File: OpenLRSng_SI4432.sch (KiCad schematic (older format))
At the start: 33 parts, among them IC1 ATMEGA328P-A, IC2 Si4432, P1 CONN_01X06, P2 CONN_02X06, P3 MML, U1 MIC5205 3,3V, Y1 RESONATEUR

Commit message: 100uF Cap von 1206 auf 1210 geändert
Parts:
- C12: footprint Capacitors_SMD:C_1206 -> Capacitors_SMD:C_1210
- C2: value 100µ -> 22u
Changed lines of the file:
@@
 LIBS:Resonator_3pins
 LIBS:OpenLRSng_SI4432-cache
-EELAYER 25 0
+EELAYER 24 0
 EELAYER END
 $Descr A4 11693 8268
@@
 P 1200 1550
 F 0 "C2" H 1200 1650 40  0000 L CNN
-F 1 "100µ" H 1206 1465 40  0000 L CNN
+F 1 "22u" H 1206 1465 40  0000 L CNN
 F 2 "Capacitors_SMD:C_1206" H 1238 1400 30  0000 C CNN
 F 3 "" H 1200 1550 60  0000 C CNN
@@
 F 0 "C12" H 6750 1200 40  0000 L CNN
 F 1 "100µ" H 6756 1015 40  0000 L CNN
-F 2 "Capacitors_SMD:C_1206" H 6788 950 30  0000 C CNN
+F 2 "Capacitors_SMD:C_1210" H 6788 950 30  0000 C CNN
 F 3 "" H 6750 1100 60  0000 C CNN
 	1    6750 1100

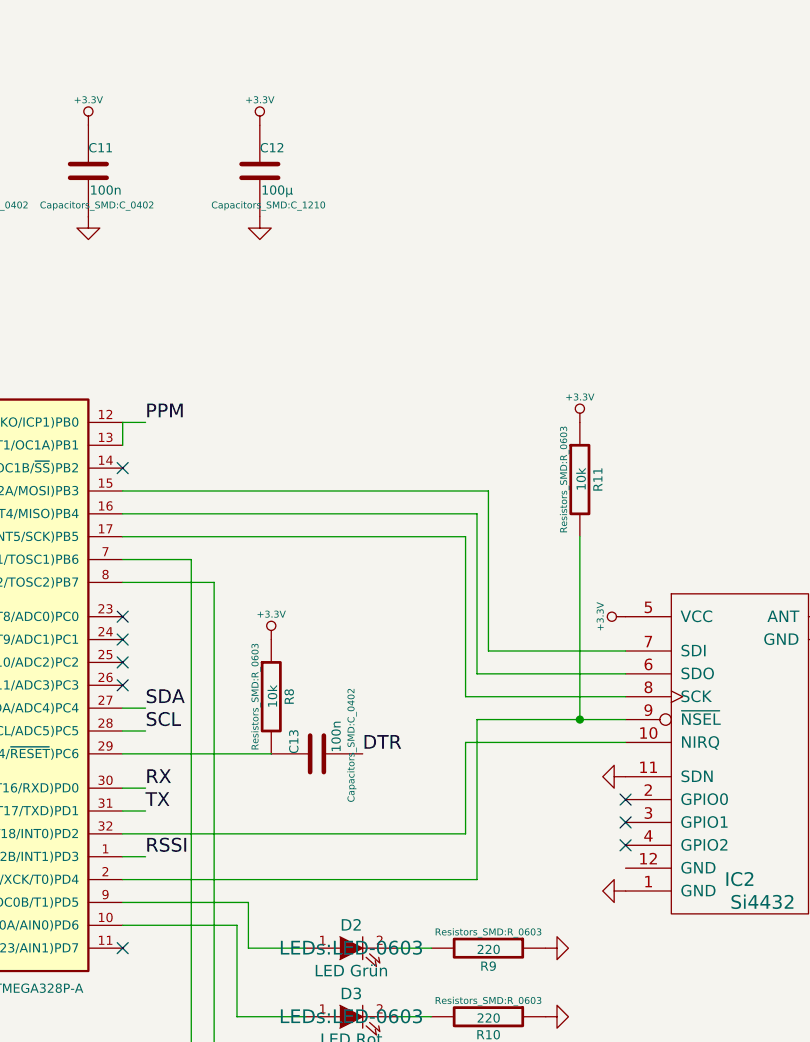
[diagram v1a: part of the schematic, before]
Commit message: -SI4432 Bibliothek gefixt (Pin14 GND vergessen im Schaltplan) -DuKo Kupferfläche vergrößert -zusätzlich noch einmal 100uF Kerko an die 3,3V Rail -Via Stichting an der Massefläche
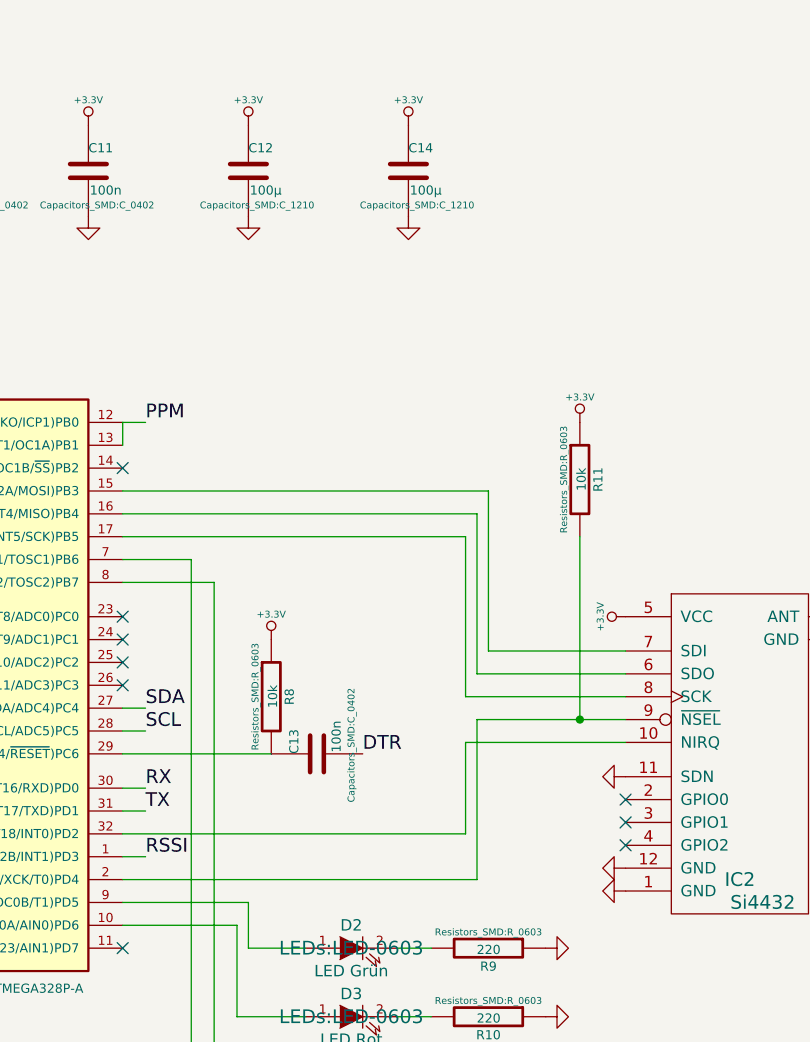
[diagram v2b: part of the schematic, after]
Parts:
- added C14: 100µ, Capacitors_SMD:C_1210, symbol C
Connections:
- net +3.3V: now also C14.1
- net GND: now also IC2.12 (GND), C14.2
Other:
- moved on the sheet: C12
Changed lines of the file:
@@
 LIBS:Resonator_3pins
 LIBS:OpenLRSng_SI4432-cache
-EELAYER 24 0
+EELAYER 25 0
 EELAYER END
 $Descr A4 11693 8268
@@
 L C C12
 U 1 1 54CDC71D
-P 6750 1100
-F 0 "C12" H 6750 1200 40  0000 L CNN
-F 1 "100µ" H 6756 1015 40  0000 L CNN
-F 2 "Capacitors_SMD:C_1210" H 6788 950 30  0000 C CNN
-F 3 "" H 6750 1100 60  0000 C CNN
-	1    6750 1100
+P 6700 1100
+F 0 "C12" H 6700 1200 40  0000 L CNN
+F 1 "100µ" H 6706 1015 40  0000 L CNN
+F 2 "Capacitors_SMD:C_1210" H 6738 950 30  0000 C CNN
+F 3 "" H 6700 1100 60  0000 C CNN
+	1    6700 1100
 	1    0    0    -1
 $EndComp
@@
 L GND #PWR045
 U 1 1 54CDCEDD
-P 6750 1300
-F 0 "#PWR045" H 6750 1300 30  0001 C CNN
-F 1 "GND" H 6750 1230 30  0001 C CNN
-F 2 "" H 6750 1300 60  0000 C CNN
-F 3 "" H 6750 1300 60  0000 C CNN
-	1    6750 1300
+P 6700 1300
+F 0 "#PWR045" H 6700 1300 30  0001 C CNN
+F 1 "GND" H 6700 1230 30  0001 C CNN
+F 2 "" H 6700 1300 60  0000 C CNN
+F 3 "" H 6700 1300 60  0000 C CNN
+	1    6700 1300
 	1    0    0    -1
 $EndComp
@@
 L +3.3V #PWR046
 U 1 1 54CDCF09
-P 6750 900
-F 0 "#PWR046" H 6750 860 30  0001 C CNN
-F 1 "+3.3V" H 6750 1010 30  0000 C CNN
-F 2 "" H 6750 900 60  0000 C CNN
-F 3 "" H 6750 900 60  0000 C CNN
-	1    6750 900
+P 6700 900
+F 0 "#PWR046" H 6700 860 30  0001 C CNN
+F 1 "+3.3V" H 6700 1010 30  0000 C CNN
+F 2 "" H 6700 900 60  0000 C CNN
+F 3 "" H 6700 900 60  0000 C CNN
+	1    6700 900
 	1    0    0    -1
 $EndComp
@@
 	-1   0    0    1
 $EndComp
+$Comp
+L C C14
+U 1 1 54D2A977
+P 7400 1100
+F 0 "C14" H 7400 1200 40  0000 L CNN
+F 1 "100µ" H 7406 1015 40  0000 L CNN
+F 2 "Capacitors_SMD:C_1210" H 7438 950 30  0000 C CNN
+F 3 "" H 7400 1100 60  0000 C CNN
+	1    7400 1100
+	1    0    0    -1
+$EndComp
+$Comp
+L GND #PWR052
+U 1 1 54D2A9F9
+P 7400 1300
+F 0 "#PWR052" H 7400 1300 30  0001 C CNN
+F 1 "GND" H 7400 1230 30  0001 C CNN
+F 2 "" H 7400 1300 60  0000 C CNN
+F 3 "" H 7400 1300 60  0000 C CNN
+	1    7400 1300
+	1    0    0    -1
+$EndComp
+$Comp
+L +3.3V #PWR053
+U 1 1 54D2AA26
+P 7400 900
+F 0 "#PWR053" H 7400 860 30  0001 C CNN
+F 1 "+3.3V" H 7400 1010 30  0000 C CNN
+F 2 "" H 7400 900 60  0000 C CNN
+F 3 "" H 7400 900 60  0000 C CNN
+	1    7400 900
+	1    0    0    -1
+$EndComp
+$Comp
+L GND #PWR054
+U 1 1 54D2C235
+P 8350 4150
+F 0 "#PWR054" H 8350 4150 30  0001 C CNN
+F 1 "GND" H 8350 4080 30  0001 C CNN
+F 2 "" H 8350 4150 60  0000 C CNN
+F 3 "" H 8350 4150 60  0000 C CNN
+	1    8350 4150
+	0    1    1    0
+$EndComp
 $EndSCHEMATC

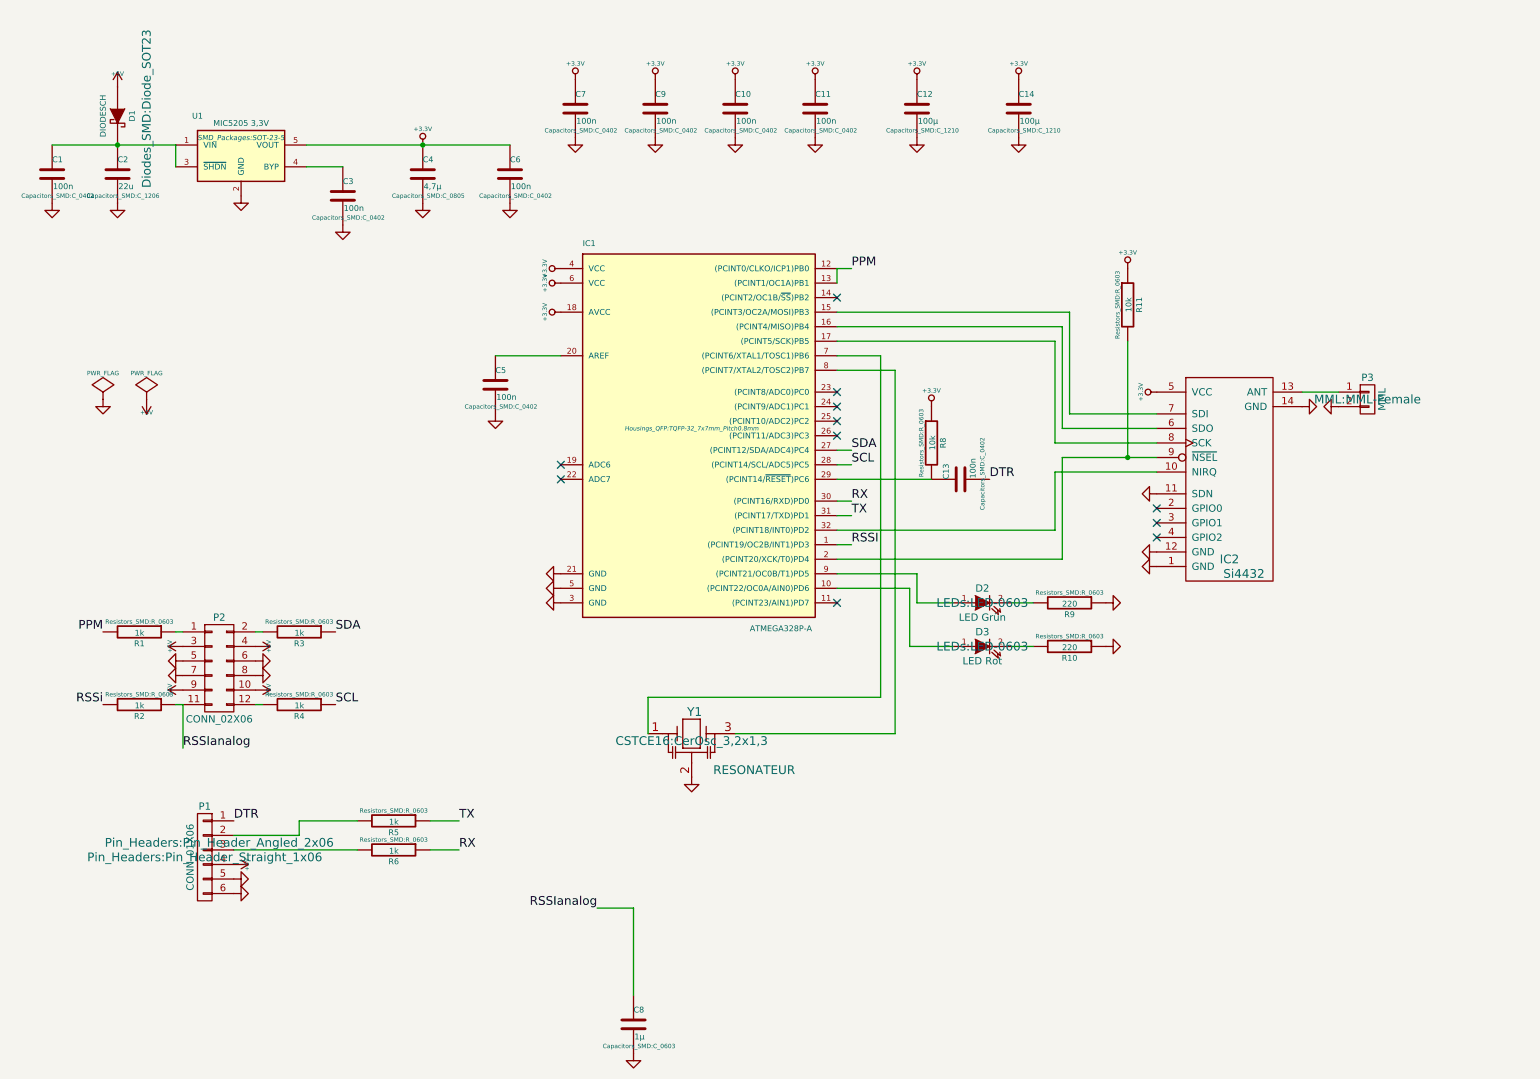
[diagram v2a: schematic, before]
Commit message: 4 Kanal auf 6 Kanal umgebaut und leicht optimiert
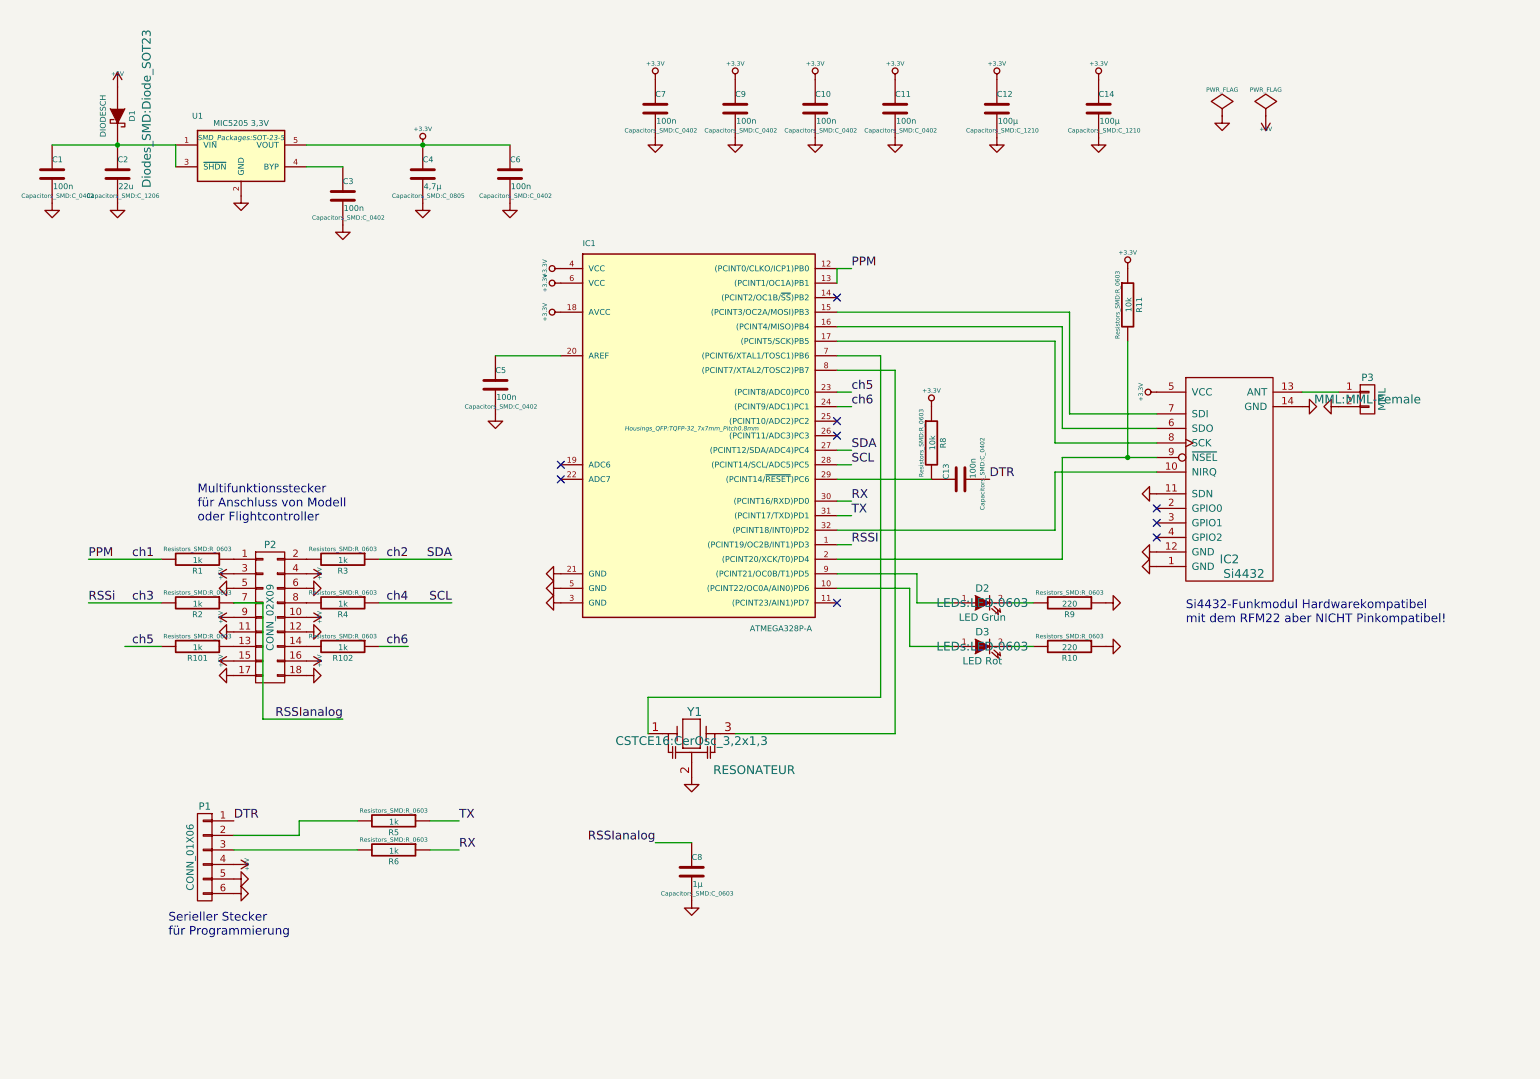
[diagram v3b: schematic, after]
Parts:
- removed P2: CONN_02X06, Pin_Headers:Pin_Header_Angled_2x06, symbol CONN_02X06
- added P2: CONN_02X09, Pin_Headers:Pin_Header_Angled_2x09, symbol CONN_02X09
- added R101, R102: 1k, Resistors_SMD:R_0603, symbol R
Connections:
- net +5V: now also P2.10 (P10), P2.15 (P15), P2.16 (P16), P2.3 (P3), P2.4 (P4), P2.9 (P9)
- net GND: now also P2.11 (P11), P2.12 (P12), P2.17 (P17), P2.18 (P18), P2.5 (P5), P2.6 (P6)
- net RSSIanalog: now also P2.7 (P7)
- net ch5: now reaches IC1.23 ((PCINT8/ADC0)PC0)
- net ch5: now also R101.2
- net ch6: now reaches IC1.24 ((PCINT9/ADC1)PC1)
- net ch6: now also R102.1
- net at R1.1: now also P2.1 (P1)
- net at R4.2: now also P2.8 (P8)
- net at R3.2: now also P2.2 (P2)
- new net: P2.13 (P13), R101.1
- new net: P2.14 (P14), R102.2
- no-connect marks 11 -> 9
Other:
- note added: "Multifunktionsstecker\nfür Anschluss von Modell\noder Flightcontroller"
- note added: "Serieller Stecker\nfür Programmierung"
- note added: "Si4432-Funkmodul Hardwarekompatibel\nmit dem RFM22 aber NICHT Pinkompatibel!"
- moved on the sheet: C10, C11, C12, C14, C7, C8, C9, R1, R2, R3, R4
